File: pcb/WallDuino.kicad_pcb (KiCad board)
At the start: 2 copper layers, 55 x 90 mm, 23 parts, among them J1 DC Jack, J2 AudioJack3_SwitchTR, J3 Motor Direction Selector, J4 Motor Connector, U1 L293D

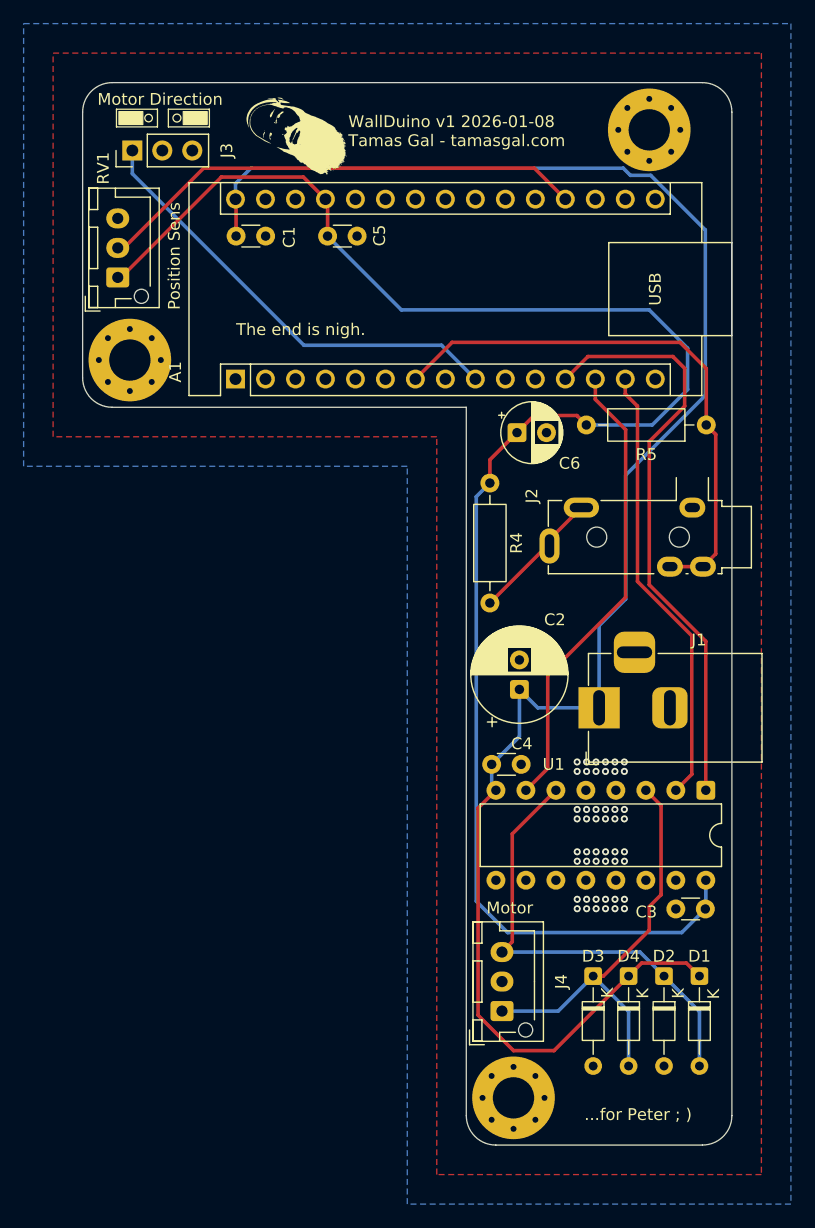
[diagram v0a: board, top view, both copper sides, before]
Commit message: Update PCB and Schematics to v1.0 Rev B
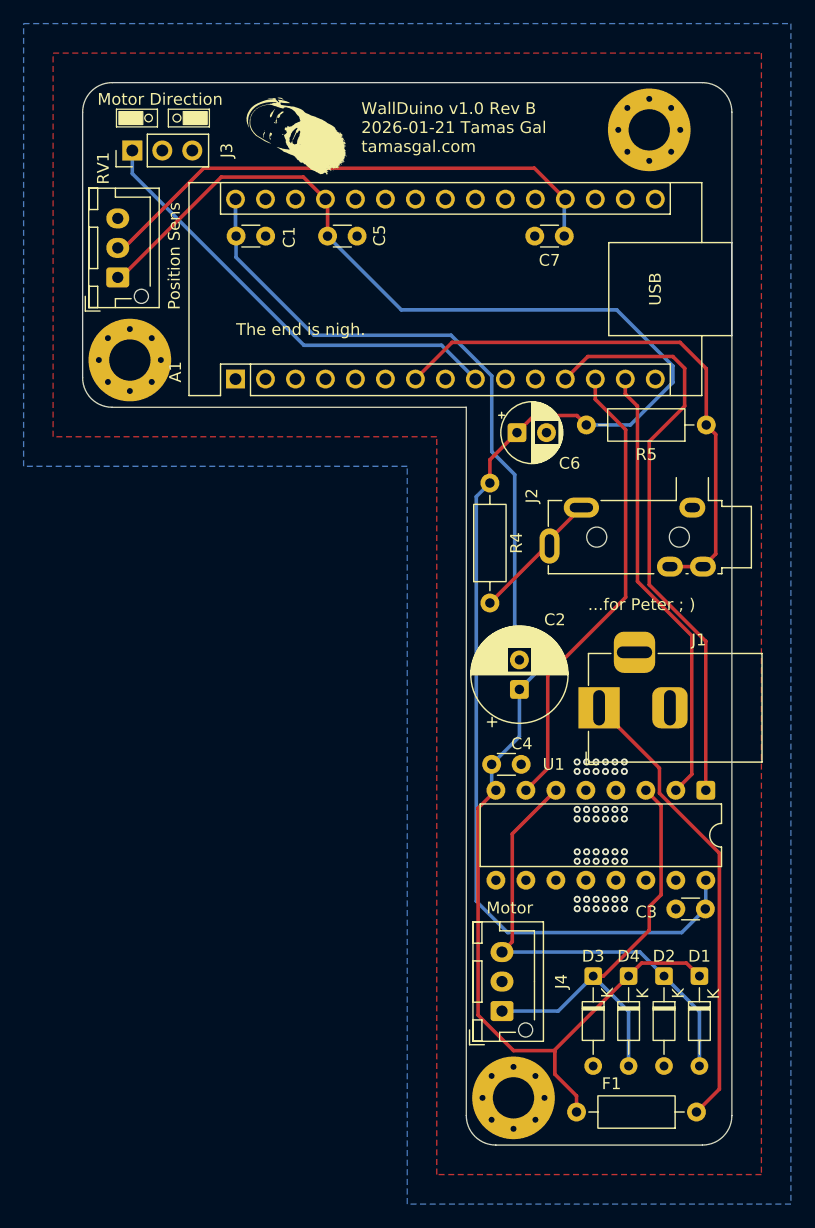
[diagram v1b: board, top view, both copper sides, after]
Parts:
- added C7: 100n, Capacitor_THT:C_Disc_D3.0mm_W1.6mm_P2.50mm, F.Cu at (155.8, 73.0)
- added F1: 750mA, Resistor_THT:R_Axial_DIN0207_L6.3mm_D2.5mm_P10.16mm_Horizontal, F.Cu at (167.0, 147.2)
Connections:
- J1 pad 1: +12V -> Net-(F1-Pad1)
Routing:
- net Net-(F1-Pad1): track 0.00 -> 39.3 mm
- net +12V: track 151.4 -> 119.1 mm
- net +5V: track 144.6 -> 140.8 mm
- net POS: track 41.8 -> 45.0 mm
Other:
- board text added: "WallDuino v1.0 Rev B 2026-01-21 Tamas Gal tamasgal.com"
- board text removed: "WallDuino v1 2026-01-08 Tamas Gal - tamasgal.com"
